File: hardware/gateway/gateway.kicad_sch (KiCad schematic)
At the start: 4 parts, among them IC1 ATTINY406-MFR, IC2 CC1101RGPR, J1 M20-9770342

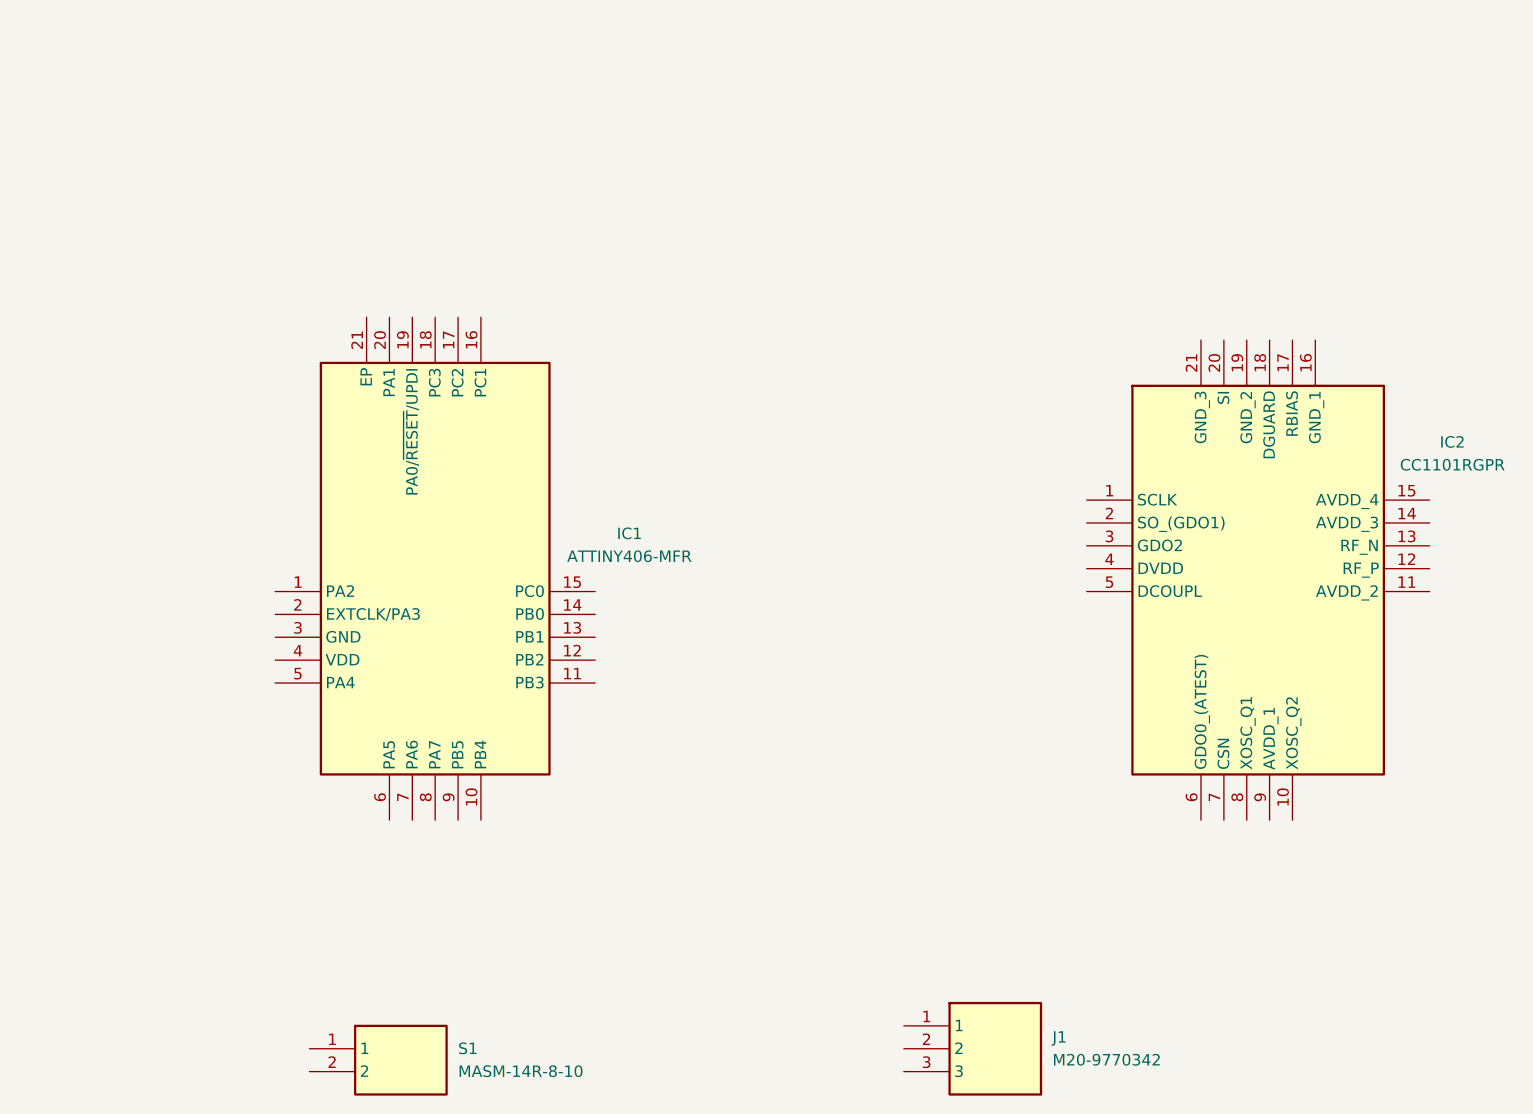
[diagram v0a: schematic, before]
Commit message: EG-11 Polarity inversion, MCU in and out interfaces connected,  including buzzer driver circuit.
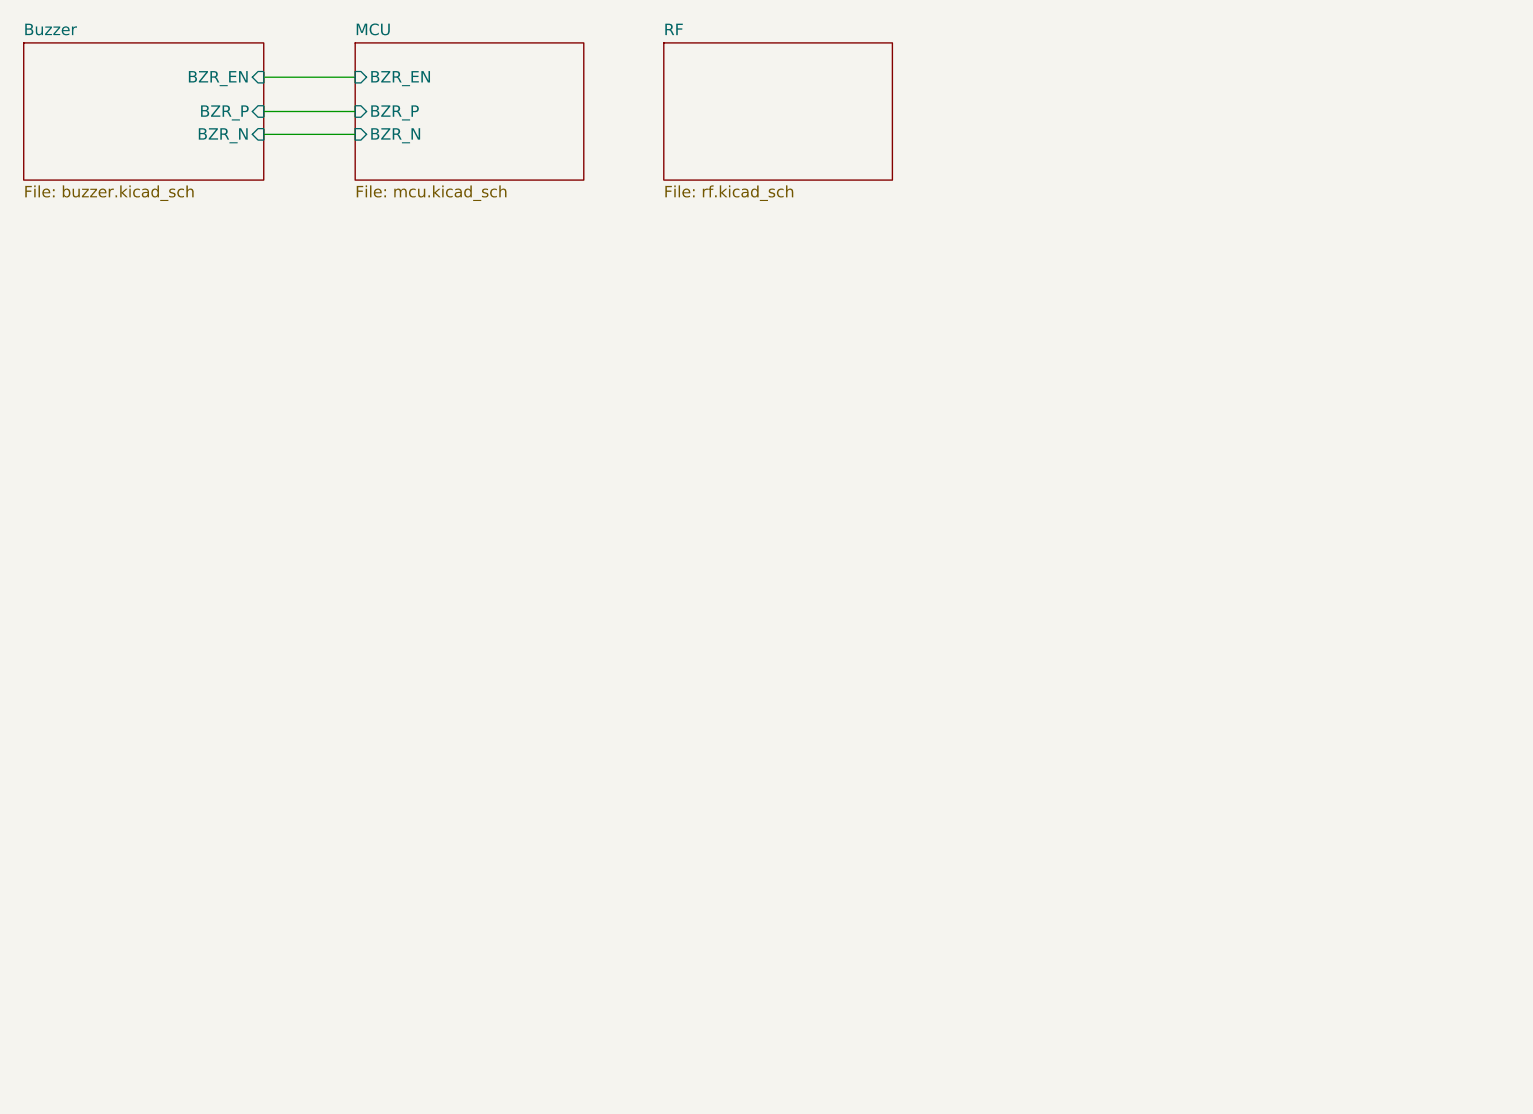
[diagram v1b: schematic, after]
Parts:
- removed IC1: ATTINY406-MFR, MyParts:QFN40P300X300X90-21N, symbol ATTINY406-MFR:ATTINY406-MFR
- removed IC2: CC1101RGPR, MyParts:QFN50P400X400X100-21N-D, symbol CC1101RGPR:CC1101RGPR
- removed J1: M20-9770342, MyParts:HDRV3W66P0X254_1X3_762X254X855P, symbol M20-9770342:M20-9770342
- removed S1: MASM-14R-8-10, MyParts:MASM14R810, symbol MASM-14R-8-10:MASM-14R-8-10
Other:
- added sheet Buzzer (buzzer.kicad_sch)
- added sheet MCU (mcu.kicad_sch)
- added sheet RF (rf.kicad_sch)

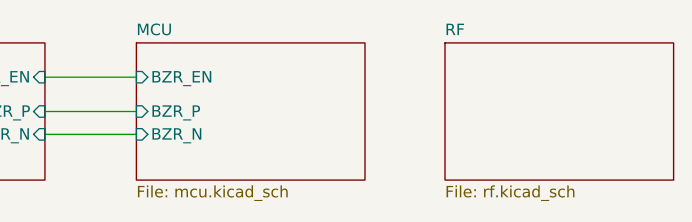
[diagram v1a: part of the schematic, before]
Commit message: EG-11 All components connected in all sheets. The MCU pin mapping needs to be fixed. The BOM needs to be created. The FRAM need needs to be assessed.
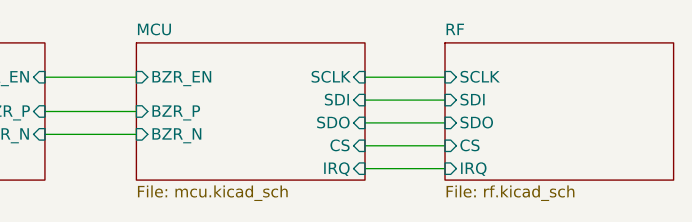
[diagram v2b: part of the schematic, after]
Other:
- sheet MCU ports: added CS, IRQ, SCLK, SDI, SDO; removed none
- sheet RF ports: added CS, IRQ, SCLK, SDI, SDO; removed none
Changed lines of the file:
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@@
+	(wire
+		(pts
+			(xy 86.36 27.94) (xy 95.25 27.94)
+		)
+		(stroke
+			(width 0)
+			(type default)
+		)
+	)
 	(wire
 		(pts
@@
 	(wire
 		(pts
+			(xy 86.36 22.86) (xy 95.25 22.86)
+		)
+		(stroke
+			(width 0)
+			(type default)
+		)
+	)
+	(wire
+		(pts
+			(xy 86.36 33.02) (xy 95.25 33.02)
+		)
+		(stroke
+			(width 0)
+			(type default)
+		)
+	)
+	(wire
+		(pts
+			(xy 86.36 30.48) (xy 95.25 30.48)
+		)
+		(stroke
+			(width 0)
+			(type default)
+		)
+	)
+	(wire
+		(pts
 			(xy 50.8 22.86) (xy 60.96 22.86)
 		)
@@
 		(pts
 			(xy 50.8 26.67) (xy 60.96 26.67)
+		)
+		(stroke
+			(width 0)
+			(type default)
+		)
+	)
+	(wire
+		(pts
+			(xy 86.36 25.4) (xy 95.25 25.4)
 		)
 		(stroke
@@
 			)
 		)
+		(pin "CS" input
+			(at 95.25 30.48 180)
+			(effects
+				(font
+					(size 1.27 1.27)
+				)
+				(justify left)
+			)
+		)
+		(pin "SCLK" input
+			(at 95.25 22.86 180)
+			(effects
+				(font
+					(size 1.27 1.27)
+				)
+				(justify left)
+			)
+		)
+		(pin "SDI" input
+			(at 95.25 25.4 180)
+			(effects
+				(font
+					(size 1.27 1.27)
+				)
+				(justify left)
+			)
+		)
+		(pin "SDO" input
+			(at 95.25 27.94 180)
+			(effects
+				(font
+					(size 1.27 1.27)
+				)
+				(justify left)
+			)
+		)
+		(pin "IRQ" input
+			(at 95.25 33.02 180)
+			(effects
+				(font
+					(size 1.27 1.27)
+				)
+				(justify left)
+			)
+		)
 		(instances
 			(project "gateway"
@@
 			)
 		)
+		(pin "CS" input
+			(at 86.36 30.48 0)
+			(effects
+				(font
+					(size 1.27 1.27)
+				)
+				(justify right)
+			)
+		)
+		(pin "SCLK" input
+			(at 86.36 22.86 0)
+			(effects
+				(font
+					(size 1.27 1.27)
+				)
+				(justify right)
+			)
+		)
+		(pin "SDI" input
+			(at 86.36 25.4 0)
+			(effects
+				(font
+					(size 1.27 1.27)
+				)
+				(justify right)
+			)
+		)
+		(pin "SDO" input
+			(at 86.36 27.94 0)
+			(effects
+				(font
+					(size 1.27 1.27)
+				)
+				(justify right)
+			)
+		)
+		(pin "IRQ" input
+			(at 86.36 33.02 0)
+			(effects
+				(font
+					(size 1.27 1.27)
+				)
+				(justify right)
+			)
+		)

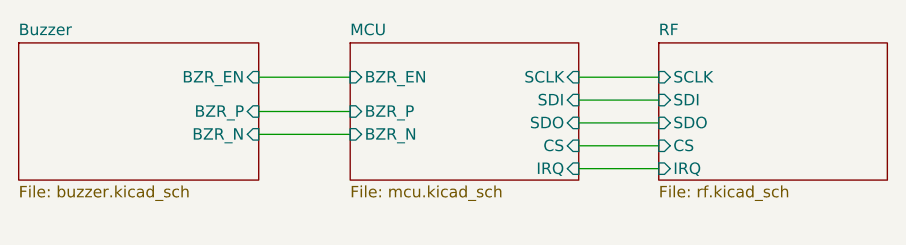
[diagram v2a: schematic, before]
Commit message: EG-11 FRAM included, MCU pin mapping finished. Only BOM is not finished.
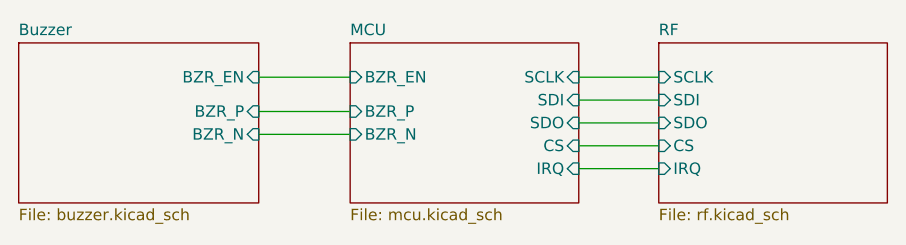
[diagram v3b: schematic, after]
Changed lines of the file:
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@@
 	(sheet
 		(at 95.25 19.05)
-		(size 25.4 15.24)
+		(size 25.4 17.78)
 		(exclude_from_sim no)
 		(in_bom yes)
@@
 		)
 		(property "Sheetfile" "rf.kicad_sch"
-			(at 95.25 34.8746 0)
+			(at 95.25 37.4146 0)
 			(effects
 				(font
@@
 	(sheet
 		(at 60.96 19.05)
-		(size 25.4 15.24)
+		(size 25.4 17.78)
 		(exclude_from_sim no)
 		(in_bom yes)
@@
 		)
 		(property "Sheetfile" "mcu.kicad_sch"
-			(at 60.96 34.8746 0)
+			(at 60.96 37.4146 0)
 			(effects
 				(font
@@
 	(sheet
 		(at 24.13 19.05)
-		(size 26.67 15.24)
+		(size 26.67 17.78)
 		(exclude_from_sim no)
 		(in_bom yes)
@@
 		)
 		(property "Sheetfile" "buzzer.kicad_sch"
-			(at 24.13 34.8746 0)
-			(effects
-				(font
+			(at 24.13 37.4146 0)
+			(effects
+				(font

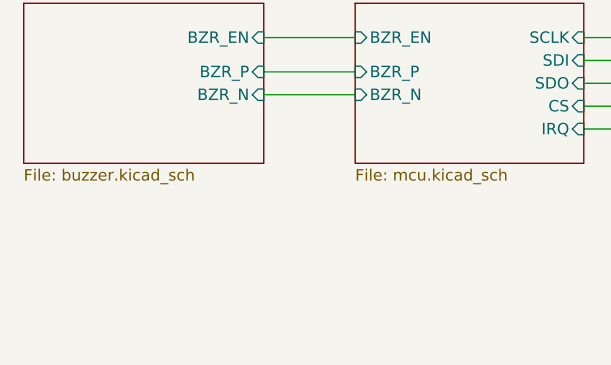
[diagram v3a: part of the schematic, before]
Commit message: EG-12 All components placed. RF connected, except antenna. Buzzer connected, buzzer power supply connected, FRAM connected. Majority os MCU connections  missing.
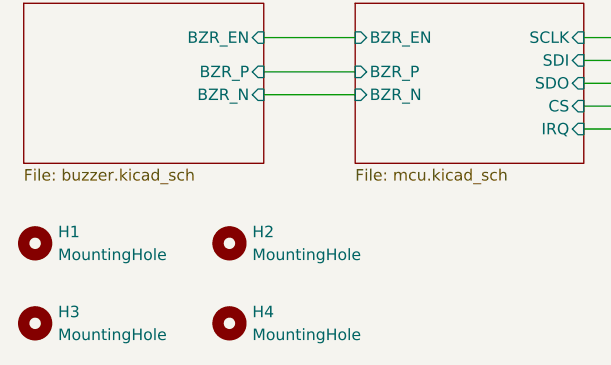
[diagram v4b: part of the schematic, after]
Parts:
- added H1, H2, H3, H4: MountingHole, MountingHole:MountingHole_2.5mm, symbol Mechanical:MountingHole
